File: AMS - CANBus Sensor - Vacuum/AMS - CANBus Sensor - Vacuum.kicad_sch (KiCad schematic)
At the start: 16 parts, among them J1 Power_And_CAN, J2 Power_And_CAN, J6 Screw_Terminal_01x02, Q1 IRF9Z34NPBF, U1 3568, U5 3568

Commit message: wip for the vacuum
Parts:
- removed J2: Power_And_CAN, TerminalBlock_Phoenix:TerminalBlock_Phoenix_MPT-0,5-4-2.54_1x04_P2.54mm_Horizontal, symbol Connector:Screw_Terminal_01x04
- removed J6: Screw_Terminal_01x02, TerminalBlock_Phoenix:TerminalBlock_Phoenix_MPT-0,5-2-2.54_1x02_P2.54mm_Horizontal, symbol Connector:Screw_Terminal_01x02
- removed RV1, RV2, RV3, RV4: 200k, Potentiometer_THT:Potentiometer_Bourns_3296W_Vertical, symbol Device:R_Potentiometer_US
- removed U1: 3568, 3568, symbol SamacSys_Parts:3568
- added C10, C8, C9: C, symbol Device:C
- added IC1: OPA2340UA_2K5, SamacSys_Parts:SOIC127P600X175-8N, symbol SamacSys_Parts:OPA2340UA_2K5
- added IC2: MCP1804T-A002I_OT, SOT95P270X145-5N, symbol SamacSys_Parts:MCP1804T-A002I_OT
- added R16: 120k, Resistor_SMD:R_1206_3216Metric_Pad1.30x1.75mm_HandSolder, symbol Device:R
- added R17: 15k, Resistor_SMD:R_1206_3216Metric_Pad1.30x1.75mm_HandSolder, symbol Device:R
- added R18: 47k, Resistor_SMD:R_1206_3216Metric_Pad1.30x1.75mm_HandSolder, symbol Device:R
- added R19: 1M, Resistor_SMD:R_1206_3216Metric_Pad1.30x1.75mm_HandSolder, symbol Device:R
- added R9: 1k, Resistor_SMD:R_0603_1608Metric, symbol Device:R_Small_US
- added U1: TL431LP, Package_TO_SOT_THT:TO-92_Inline, symbol Reference_Voltage:TL431LP
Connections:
- net +5V: now also IC1.8 (V+), R9.1
- net +VDC: now also C8.1, IC2.1 (VIN), IC2.4 (~{SHDN}), R16.1
- net GND: now also C10.2, C8.2, C9.2, IC1.4 (V-), IC2.2 (GND), R17.2, R18.2, R19.2, U1.2 (A)
- new net: IC1.1 (OUT_A), IC1.2 (-INA), R18.1
- new net: IC1.3 (+IN_A), R16.2, R17.1
- new net +10V: C9.1, IC2.5 (VOUT)
- new net +2V5: C10.1, IC1.5 (+INB), R9.2, U1.1 (REF), U1.3 (K)
- new net VacuumSensor1/2.5V: IC1.6 (-IN_B), IC1.7 (OUTB), R19.1
- no-connect marks 12 -> 3
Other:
- removed sheet BufferedADC
- added sheet VacuumSensor1 (VacuumSensor.kicad_sch)
- added sheet VacuumSensor2 (VacuumSensor.kicad_sch)
- moved on the sheet: NTC1, R2, R3, Reset1

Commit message: i think the Vacuum sensor is done i need to test s afew things and then this is ready for fab
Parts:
- added R12, R13: 10k, Resistor_SMD:R_1206_3216Metric_Pad1.30x1.75mm_HandSolder, symbol Device:R
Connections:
- net +5V: now also R12.1, R13.1
- net ADS1115/AIN3: now reaches IC1.1 (OUT_A), IC1.2 (-INA), R18.1
- net VacuumSensor1/2.5V renamed ADS1115/AIN0
- new net SCLB: R13.2
- new net SDAB: R12.2
- no-connect marks 3 -> 2
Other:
- added sheet ADS1115 (ADS1115.kicad_sch)

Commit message: vacuum wip
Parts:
- C10: value C -> 22nF; footprint (none) -> Capacitor_SMD:C_1206_3216Metric_Pad1.33x1.80mm_HandSolder
- C8: value C -> 10uF; footprint (none) -> Capacitor_SMD:C_0603_1608Metric_Pad1.08x0.95mm_HandSolder
- C9: value C -> 22uF; footprint (none) -> Capacitor_SMD:C_0603_1608Metric_Pad1.08x0.95mm_HandSolder
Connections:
- no-connect marks 2 -> 13
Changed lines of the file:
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@@
 	)
 	(no_connect
+		(at 191.77 110.49)
+	)
+	(no_connect
+		(at 191.77 107.95)
+	)
+	(no_connect
+		(at 191.77 115.57)
+	)
+	(no_connect
+		(at 191.77 90.17)
+	)
+	(no_connect
+		(at 226.06 95.25)
+	)
+	(no_connect
 		(at 281.94 119.38)
 	)
 	(no_connect
+		(at 226.06 97.79)
+	)
+	(no_connect
 		(at 281.94 116.84)
 	)
+	(no_connect
+		(at 191.77 100.33)
+	)
+	(no_connect
+		(at 191.77 92.71)
+	)
+	(no_connect
+		(at 191.77 102.87)
+	)
+	(no_connect
+		(at 226.06 92.71)
+	)
+	(no_connect
+		(at 191.77 105.41)
+	)
 	(wire
 		(pts
@@
 	(wire
 		(pts
+			(xy 148.59 97.79) (xy 191.77 97.79)
+		)
+		(stroke
+			(width 0)
+			(type default)
+		)
+	)
+	(wire
+		(pts
 			(xy 127 64.77) (xy 127 66.04)
 		)
@@
 	(wire
 		(pts
+			(xy 148.59 133.35) (xy 148.59 97.79)
+		)
+		(stroke
+			(width 0)
+			(type default)
+		)
+	)
+	(wire
+		(pts
 			(xy 39.37 128.27) (xy 50.8 128.27)
 		)
@@
 	(wire
 		(pts
+			(xy 114.3 133.35) (xy 148.59 133.35)
+		)
+		(stroke
+			(width 0)
+			(type default)
+		)
+	)
+	(wire
+		(pts
 			(xy 240.03 53.34) (xy 240.03 50.8)
 		)
@@
 			)
 		)
-		(property "Value" "C"
+		(property "Value" "22nF"
 			(at 44.45 87.6299 0)
 			(effects
@@
 			)
 		)
-		(property "Footprint" ""
+		(property "Footprint" "Capacitor_SMD:C_1206_3216Metric_Pad1.33x1.80mm_HandSolder"
 			(at 41.6052 90.17 0)
 			(effects
@@
 			)
 		)
-		(property "Value" "C"
+		(property "Value" "10uF"
 			(at 64.77 91.4399 0)
 			(effects
@@
 			)
 		)
-		(property "Footprint" ""
+		(property "Footprint" "Capacitor_SMD:C_0603_1608Metric_Pad1.08x0.95mm_HandSolder"
 			(at 61.9252 93.98 0)
 			(effects
@@
 			)
 		)
-		(property "Value" "C"
+		(property "Value" "22uF"
 			(at 109.22 101.5999 0)
 			(effects
@@
 			)
 		)
-		(property "Footprint" ""
+		(property "Footprint" "Capacitor_SMD:C_0603_1608Metric_Pad1.08x0.95mm_HandSolder"
 			(at 106.3752 104.14 0)
 			(effects

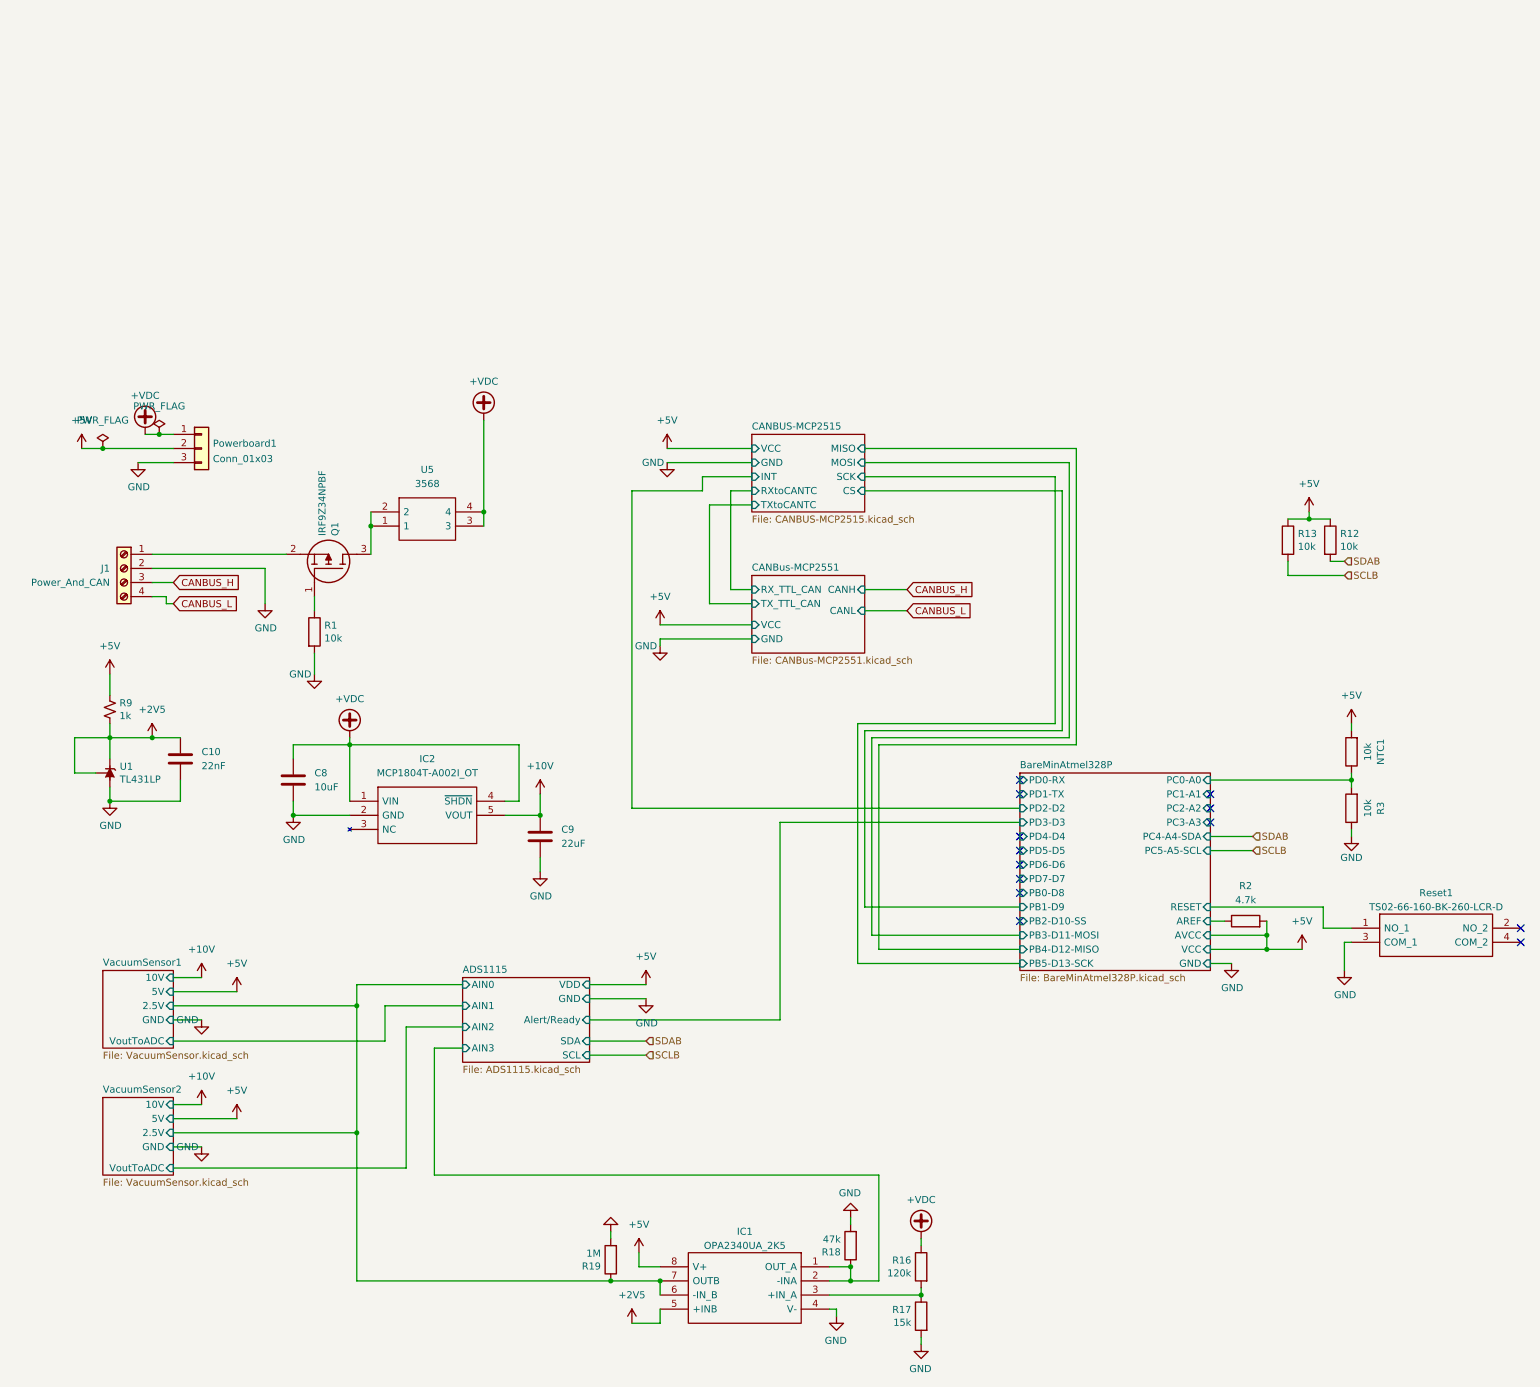
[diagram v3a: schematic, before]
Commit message: removing the 2.5v ref and putting in -5v rail. need to prototype this out to viability
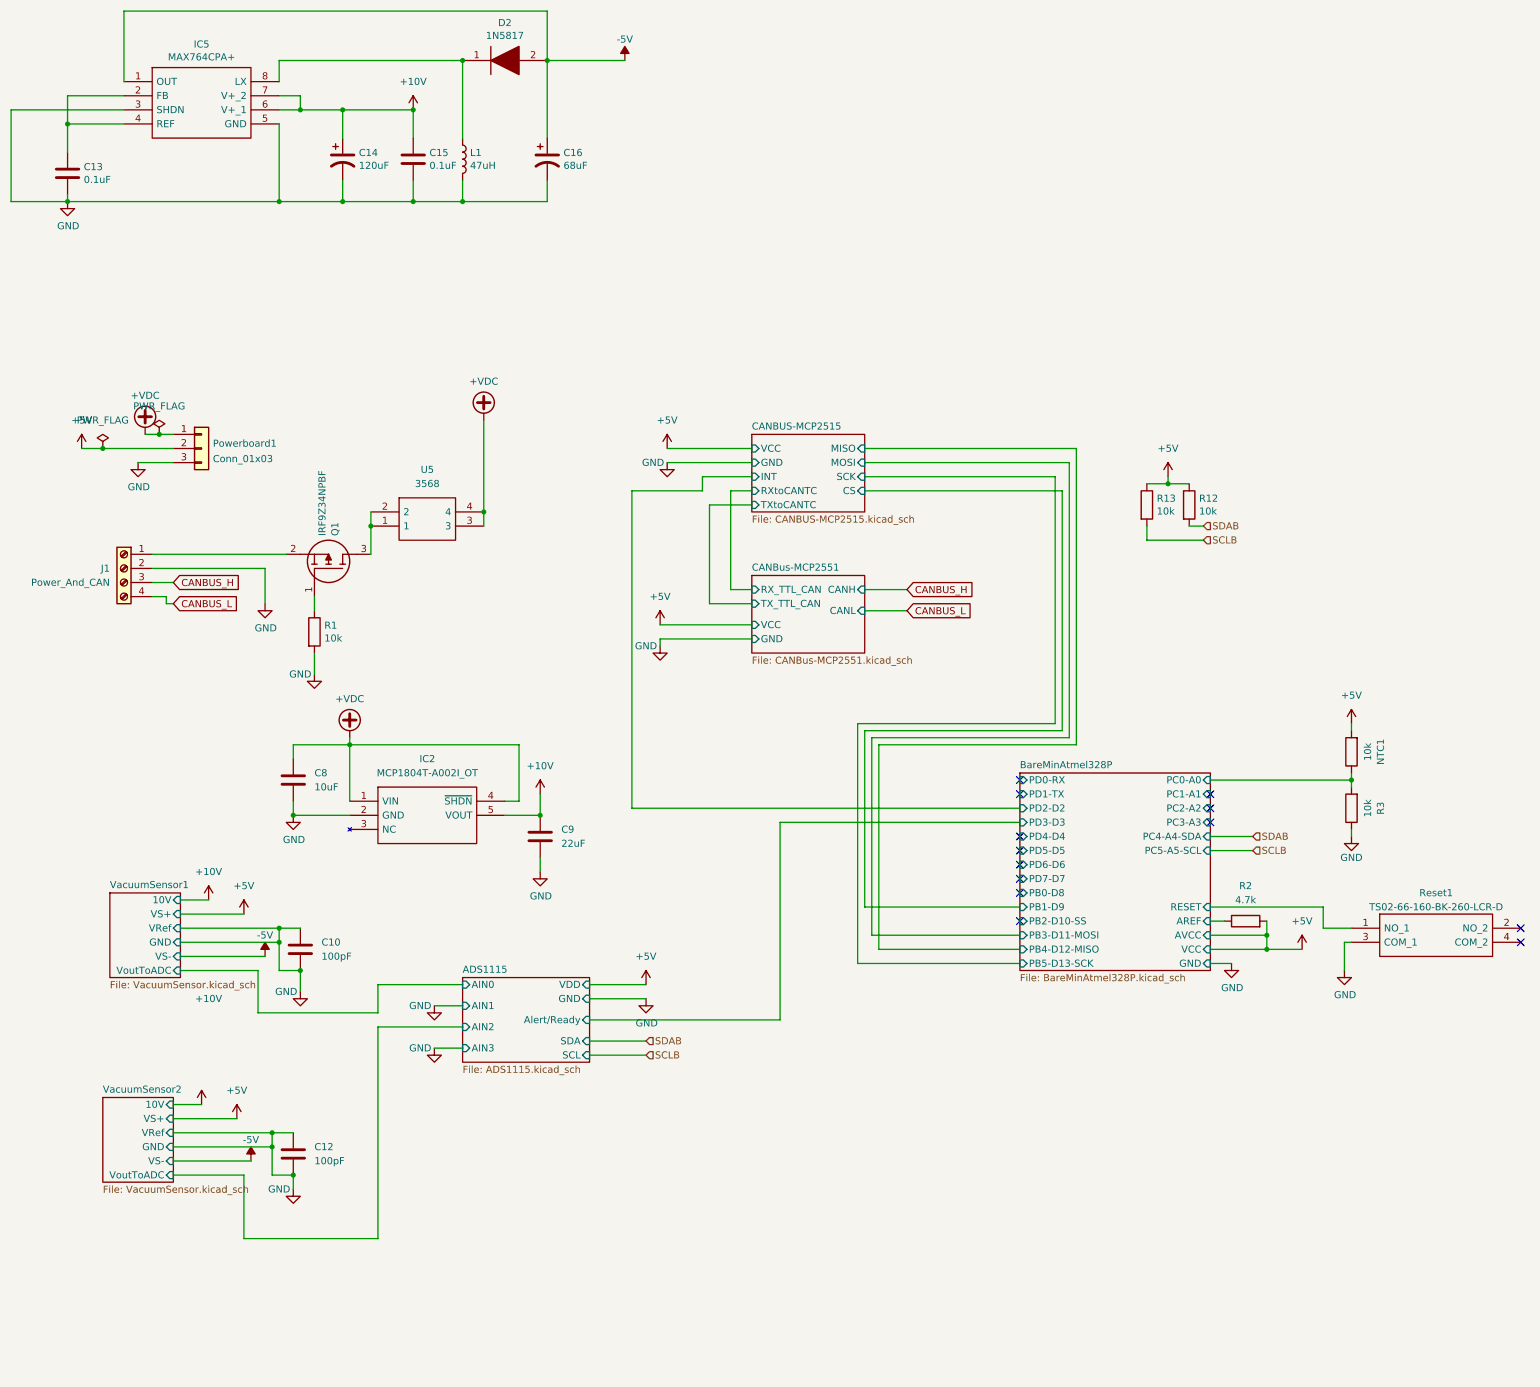
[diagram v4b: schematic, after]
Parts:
- removed IC1: OPA2340UA_2K5, SamacSys_Parts:SOIC127P600X175-8N, symbol SamacSys_Parts:OPA2340UA_2K5
- removed R16: 120k, Resistor_SMD:R_1206_3216Metric_Pad1.30x1.75mm_HandSolder, symbol Device:R
- removed R17: 15k, Resistor_SMD:R_1206_3216Metric_Pad1.30x1.75mm_HandSolder, symbol Device:R
- removed R18: 47k, Resistor_SMD:R_1206_3216Metric_Pad1.30x1.75mm_HandSolder, symbol Device:R
- removed R19: 1M, Resistor_SMD:R_1206_3216Metric_Pad1.30x1.75mm_HandSolder, symbol Device:R
- removed R9: 1k, Resistor_SMD:R_0603_1608Metric, symbol Device:R_Small_US
- removed U1: TL431LP, Package_TO_SOT_THT:TO-92_Inline, symbol Reference_Voltage:TL431LP
- added C12: 100pF, Capacitor_SMD:C_0603_1608Metric_Pad1.08x0.95mm_HandSolder, symbol Device:C
- added C13, C15: 0.1uF, Capacitor_SMD:C_0603_1608Metric_Pad1.08x0.95mm_HandSolder, symbol Device:C
- added C14: 120uF, Capacitor_THT:CP_Radial_D8.0mm_P5.00mm, symbol Device:CP1
- added C16: 68uF, Capacitor_THT:CP_Radial_D8.0mm_P5.00mm, symbol Device:CP1
- added D2: 1N5817, SamacSys_Parts:DIOAD1414W86L464D238, symbol SamacSys_Parts:1N5817
- added IC5: MAX764CPA+, SamacSys_Parts:DIP762W56P254L938H457Q8N, symbol SamacSys_Parts:MAX764CPA+
- added L1: 47uH, Inductor_THT:L_Axial_L7.0mm_D3.3mm_P10.16mm_Horizontal_Fastron_MICC, symbol Device:L
- C10: value 22nF -> 100pF; footprint Capacitor_SMD:C_1206_3216Metric_Pad1.33x1.80mm_HandSolder -> Capacitor_SMD:C_0603_1608Metric_Pad1.08x0.95mm_HandSolder
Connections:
- net +2V5 is gone; now on net GND: C10.1
- net +10V: now also C14.1, C15.1, IC5.6 (V+_1), IC5.7 (V+_2)
- net GND: now also C12.1, C12.2, C13.2, C14.2, C15.2, C16.2, IC5.3 (SHDN), IC5.5 (GND), L1.2
- new net: D2.1, IC5.8 (LX), L1.1
- new net: C13.1, IC5.2 (FB), IC5.4 (REF)
- new net -5V: C16.1, D2.2, IC5.1 (OUT)
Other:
- sheet VacuumSensor1 ports: added VRef, VS+, VS-; removed 2.5V, 5V
- sheet VacuumSensor2 ports: added VRef, VS+, VS-; removed 2.5V, 5V
- moved on the sheet: R12, R13
